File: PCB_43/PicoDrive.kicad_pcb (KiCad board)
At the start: 2 copper layers, 75.2 x 57.6 mm, 28 parts, among them J1 Conn_02x08_Row_Letter_Last, J3 OLED SCREEN CONN, J4 Micro_SD_Card_Det1, Q3 2N2219, U1 Pico, U2 TSR_1-2450

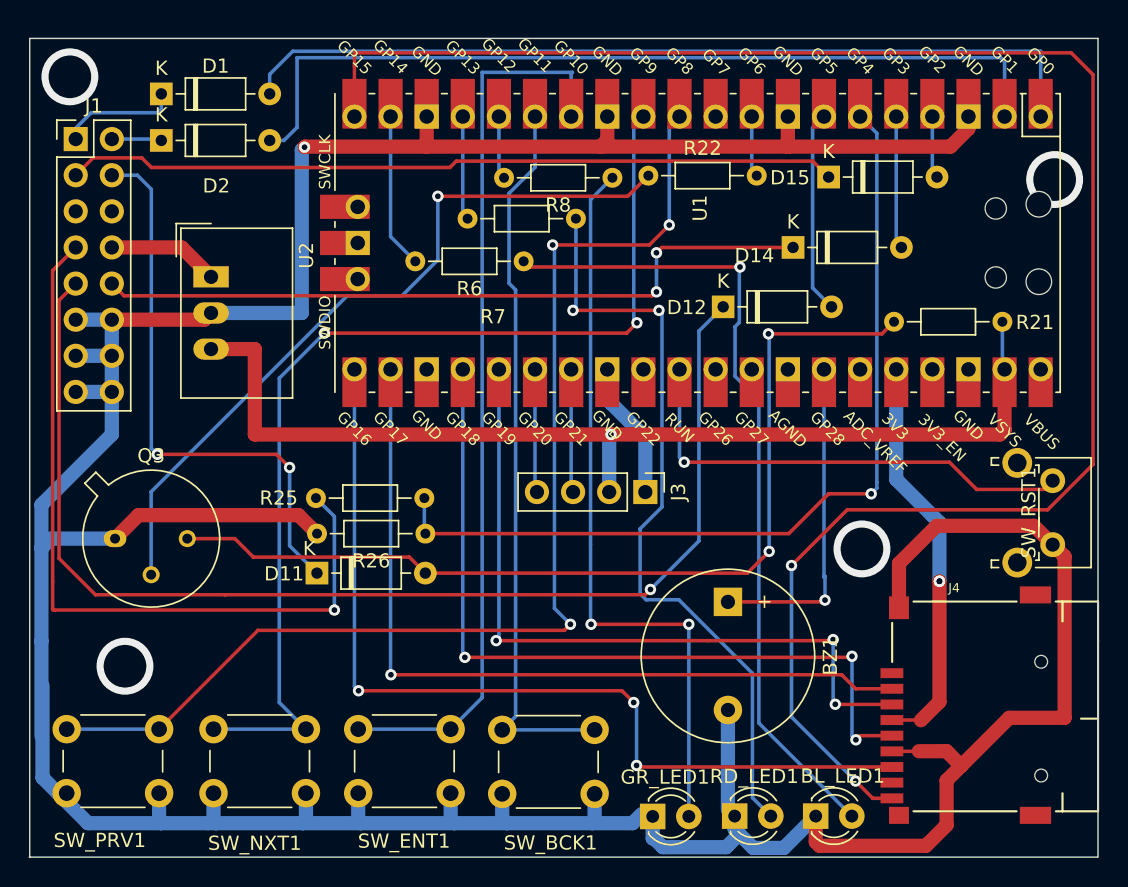
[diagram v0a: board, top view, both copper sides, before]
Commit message: Added to PCB a connector for MDV_Control boards
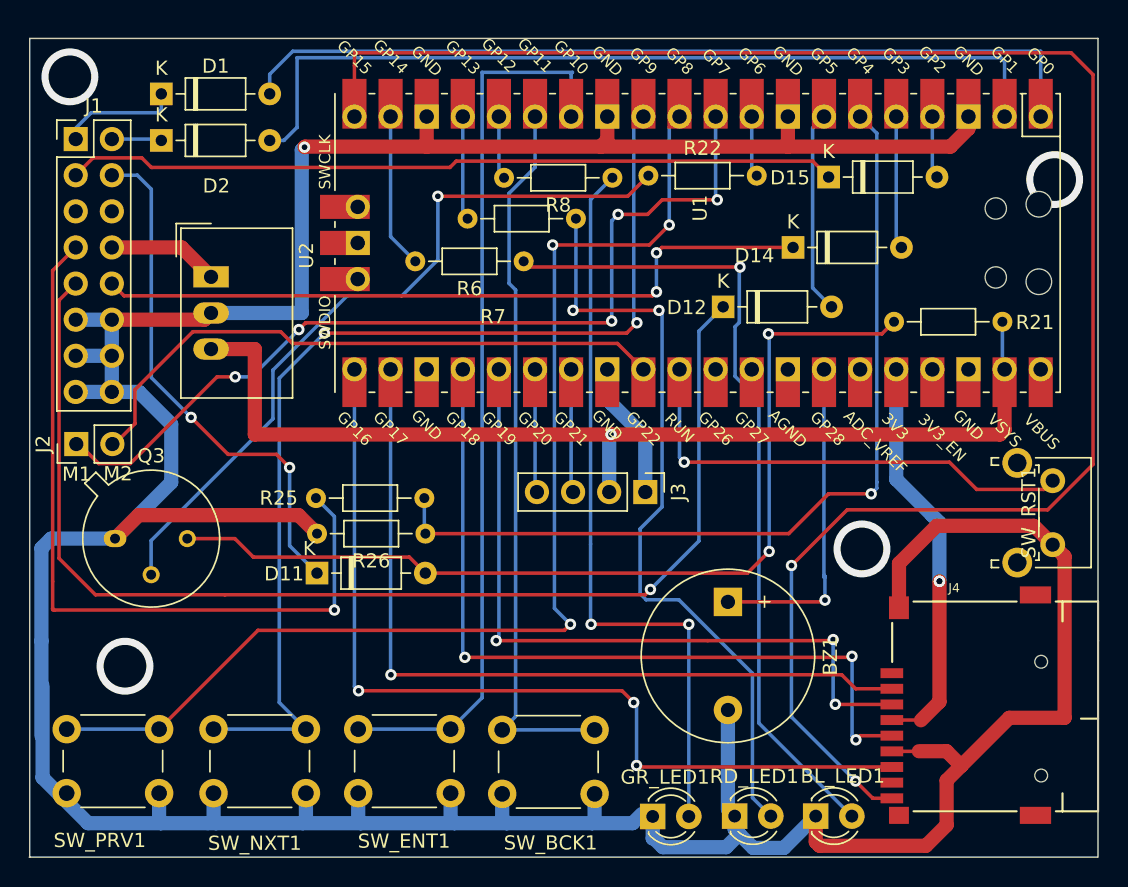
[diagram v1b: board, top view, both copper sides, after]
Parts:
- added J2: MDV_CONTROL, Connector_PinHeader_2.54mm:PinHeader_1x02_P2.54mm_Vertical, F.Cu at (93.2, 101.3)
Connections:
- U1 pad 10: unconnected-(U1-GPIO7-Pad10) -> Net-(J2-Pin_1)
- U1 pad 29: unconnected-(U1-GPIO22-Pad29) -> Net-(J2-Pin_2)
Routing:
- net Net-(J2-Pin_1): track 0.00 -> 63.2 mm, vias 0 -> 5
- net Net-(J2-Pin_2): track 0.00 -> 42.9 mm
- net Net-(D11-K): track 40.0 -> 37.1 mm
- net /GND: track 290.7 -> 292.5 mm
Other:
- board text added: "M1"
- board text added: "M2"
